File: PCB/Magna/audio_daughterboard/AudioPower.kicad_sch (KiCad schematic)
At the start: 24 parts, among them U901 TPS61040DBV, U902 AMS1117-5.0

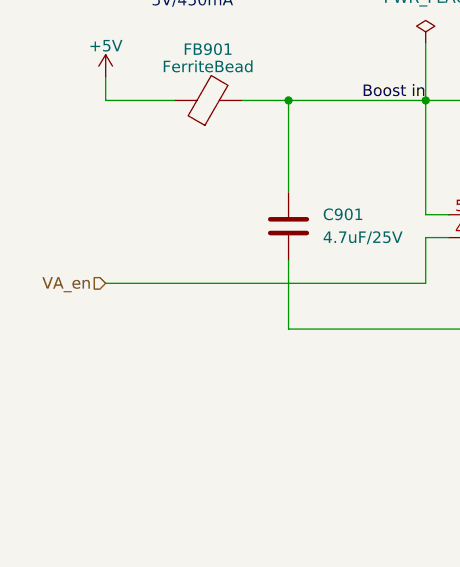
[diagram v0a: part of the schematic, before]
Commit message: Update connector on ADC board and clean up MCU sheet
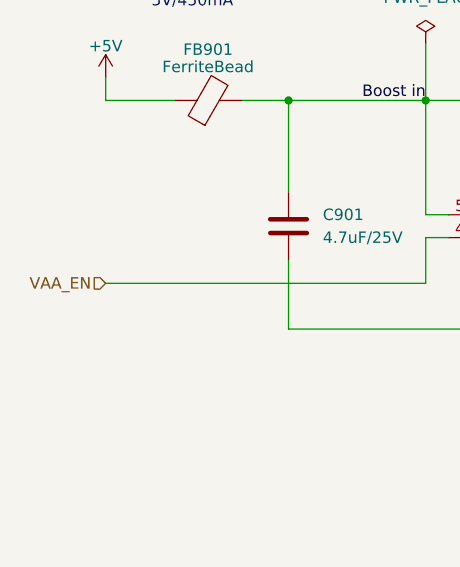
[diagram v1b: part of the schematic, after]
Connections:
- net VA_en renamed VAA_EN
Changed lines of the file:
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@@
     (effects (font (size 1.27 1.27)) (justify right bottom))
   )
-  (hierarchical_label "VA_en" (shape input) (at 26.67 129.54 180) (fields_autoplaced)
+  (hierarchical_label "VAA_EN" (shape input) (at 26.67 129.54 180) (fields_autoplaced)
     (effects (font (size 1.27 1.27)) (justify right))
   )

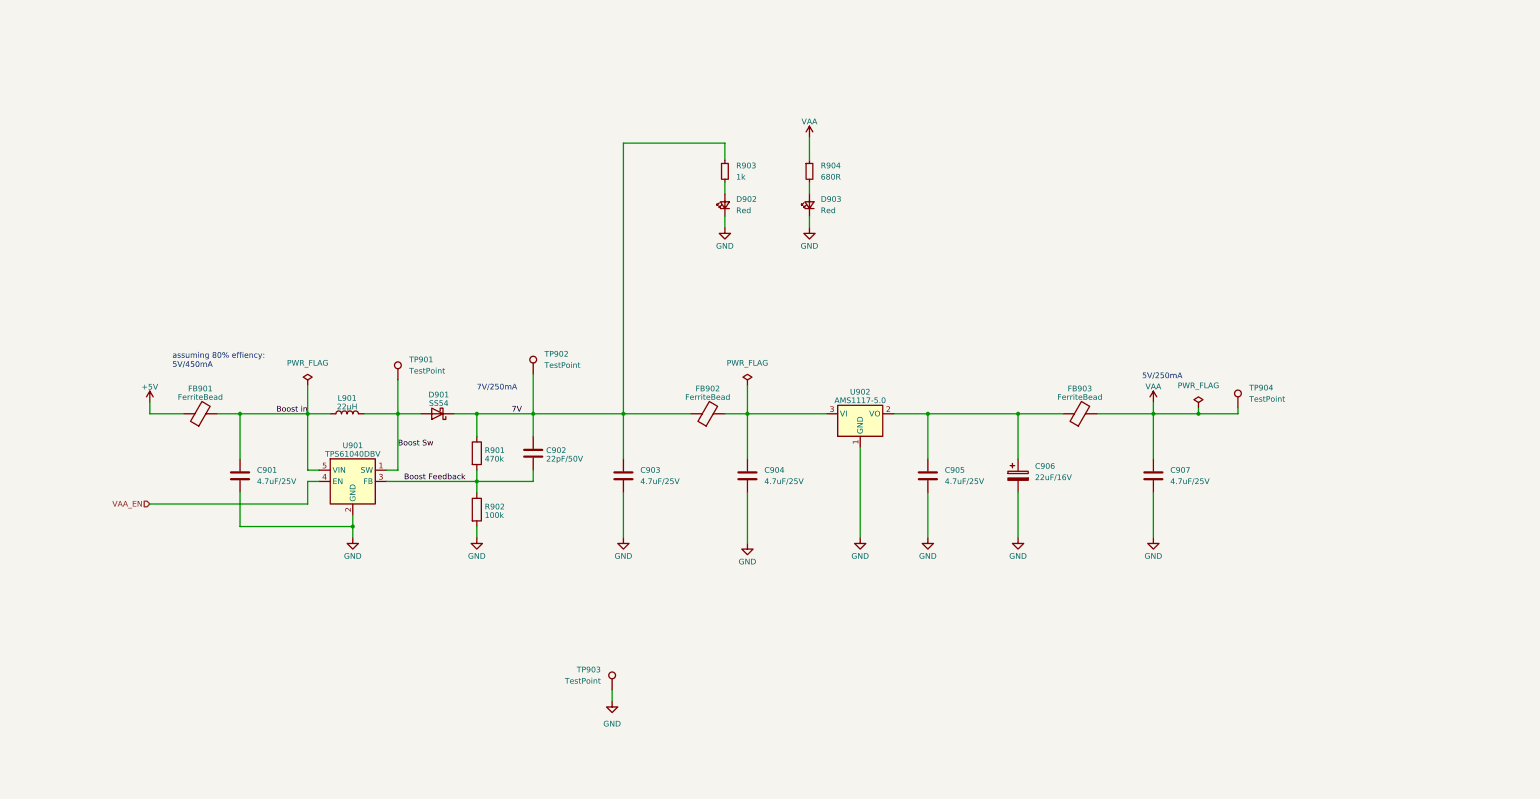
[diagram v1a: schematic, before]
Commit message: Start of redesign of Audio board
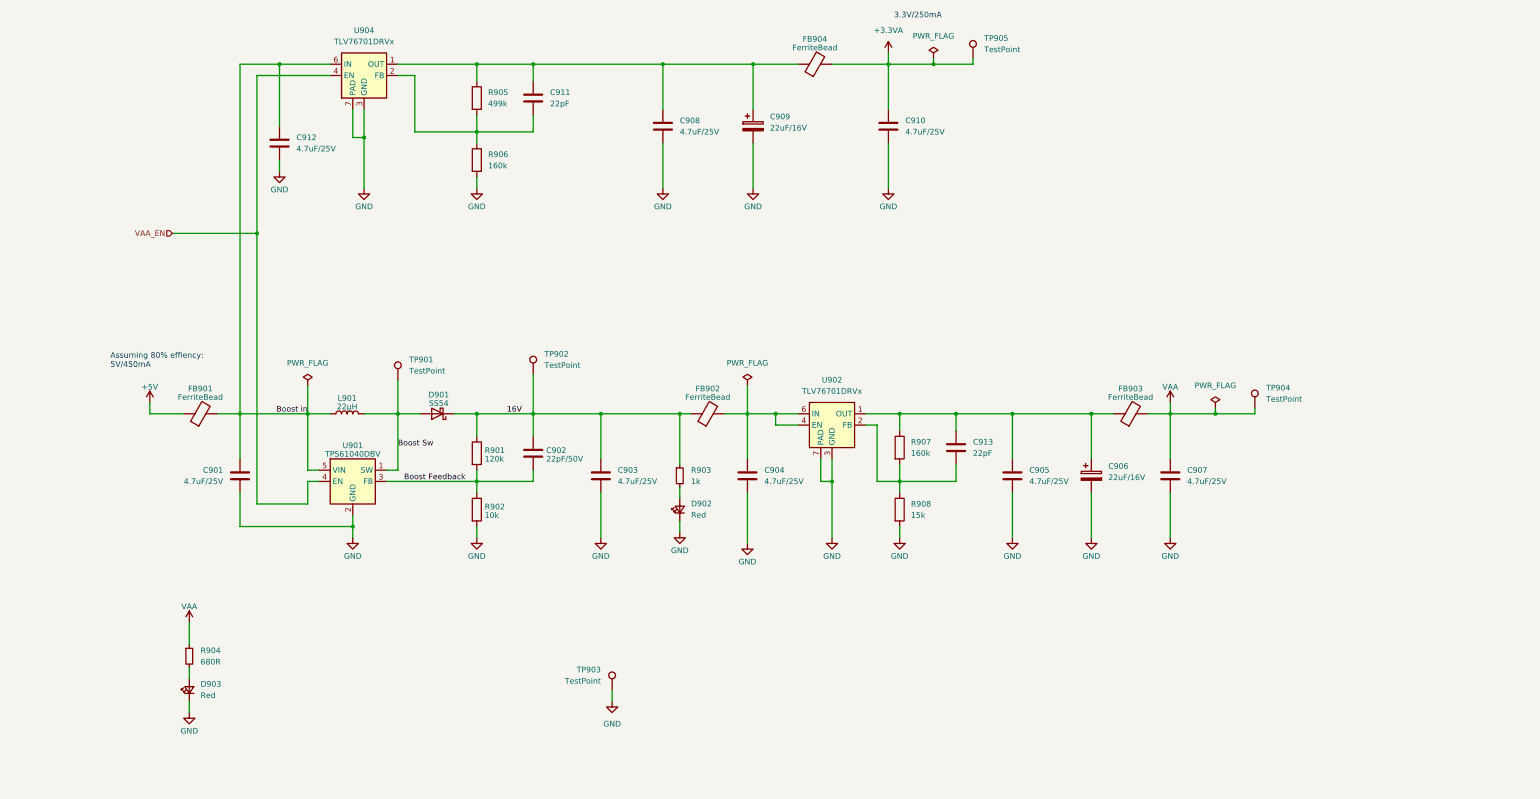
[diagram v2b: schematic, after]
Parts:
- removed U902: AMS1117-5.0, Package_TO_SOT_SMD:SOT-223-3_TabPin2, symbol Regulator_Linear:AMS1117-5.0
- added C908, C910, C912: 4.7uF/25V, Capacitor_SMD:C_0805_2012Metric_Pad1.18x1.45mm_HandSolder, symbol Device:C
- added C909: 22uF/16V, Capacitor_SMD:CP_Elec_5x5.8, symbol Device:C_Polarized
- added C911, C913: 22pF, symbol Device:C
- added FB904: FerriteBead, Inductor_SMD:L_0805_2012Metric, symbol Device:FerriteBead
- added R905: 499k, symbol Device:R
- added R906, R907: 160k, symbol Device:R
- added R908: 15k, symbol Device:R
- added TP905: TestPoint, TestPoint:TestPoint_Keystone_5005-5009_Compact, symbol Connector:TestPoint
- added U902, U904: TLV76701DRVx, Package_SON:WSON-6-1EP_2x2mm_P0.65mm_EP1x1.6mm_ThermalVias, symbol Regulator_Linear:TLV76701DRVx
- R901: value 470k -> 120k
- R902: value 100k -> 10k
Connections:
- net Boost in: now also C912.1, U904.6 (IN)
- net GND: now also C908.2, C909.2, C910.2, C912.2, R906.2, R908.2, U902.3 (GND), U902.5 (GND), U902.7 (PAD), U904.3 (GND), U904.5 (GND), U904.7 (PAD)
- net VAA_EN: now also U904.4 (EN)
- net at C905.1, C906.1, FB903.1: now also C913.1, R907.1, U902.1 (OUT)
- net at C904.1, FB902.2: now also U902.4 (EN), U902.6 (IN)
- net 7V renamed 16V
- new net: C908.1, C909.1, C911.1, FB904.1, R905.1, U904.1 (OUT)
- new net: C911.2, R905.2, R906.1, U904.2 (FB)
- new net: C913.2, R907.2, R908.1, U902.2 (FB)
- new net +3.3VA: C910.1, FB904.2, TP905.1
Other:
- note added: "3.3V/250mA"
- note added: "Assuming 80% effiency: 5V/450mA"
- note removed: "5V/250mA"
- note removed: "7V/250mA"
- note removed: "assuming 80% effiency: 5V/450mA"
- moved on the sheet: C903, C905, C906, C907, D902, D903, FB903, R903, R904, TP904

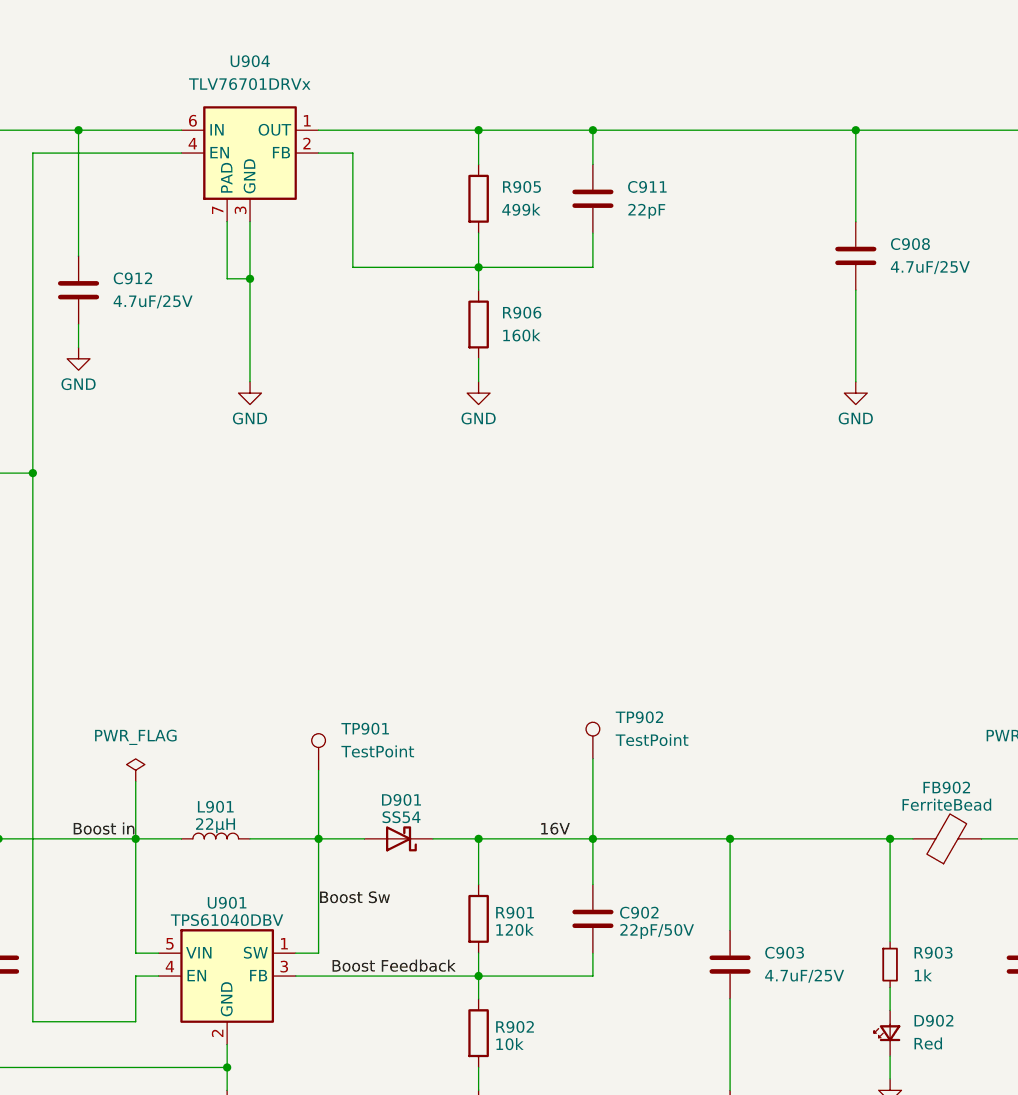
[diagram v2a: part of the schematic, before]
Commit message: Add simulation to all components
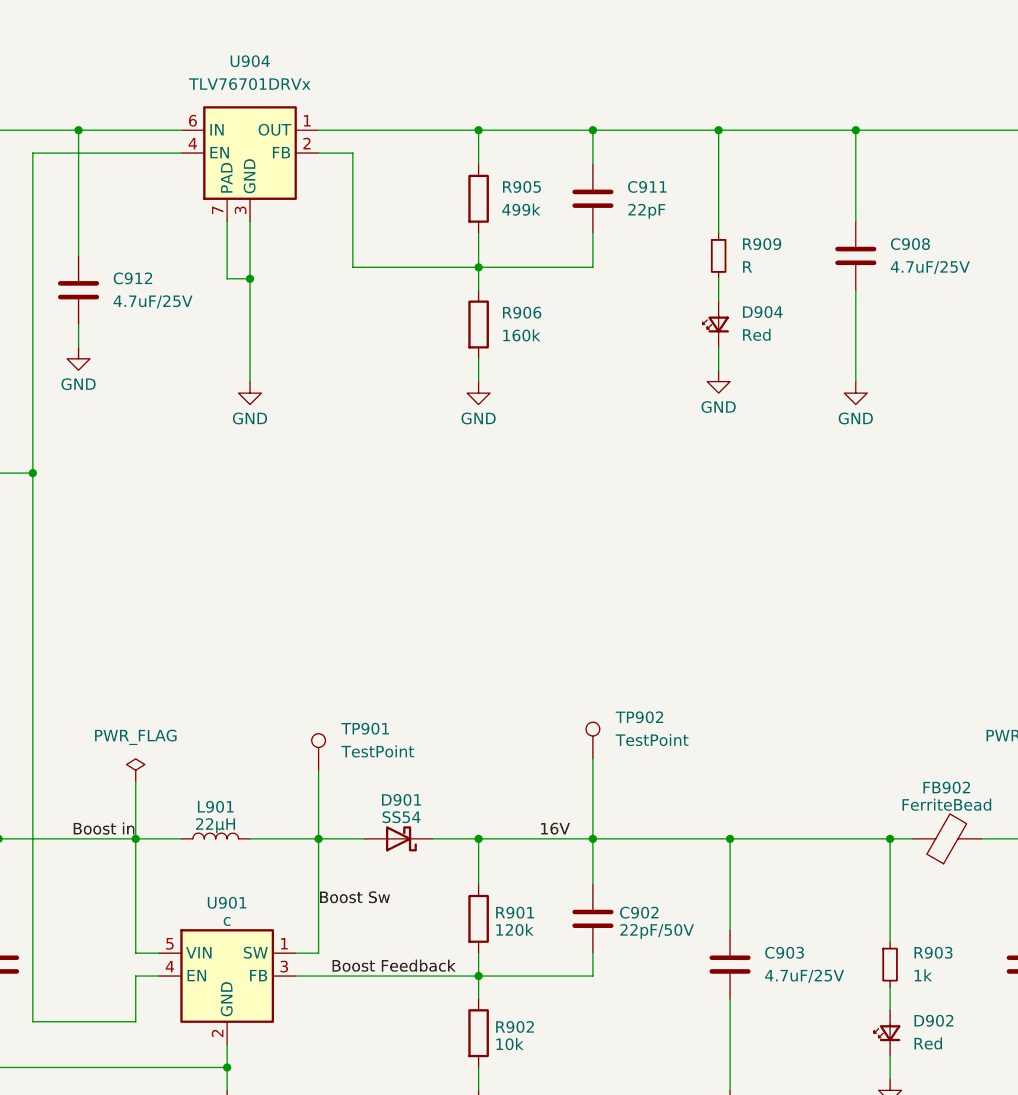
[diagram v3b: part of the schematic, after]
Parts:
- added D904: Red, Diode_SMD:D_0805_2012Metric_Pad1.15x1.40mm_HandSolder, symbol Device:LED_Small
- added R909: R, Resistor_SMD:R_0805_2012Metric_Pad1.20x1.40mm_HandSolder, symbol Device:R_Small
- U901: value TPS61040DBV -> c
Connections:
- net GND: now also D904.1 (K)
- net at C908.1, C909.1, C911.1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: now also R909.1
- new net: D904.2 (A), R909.2

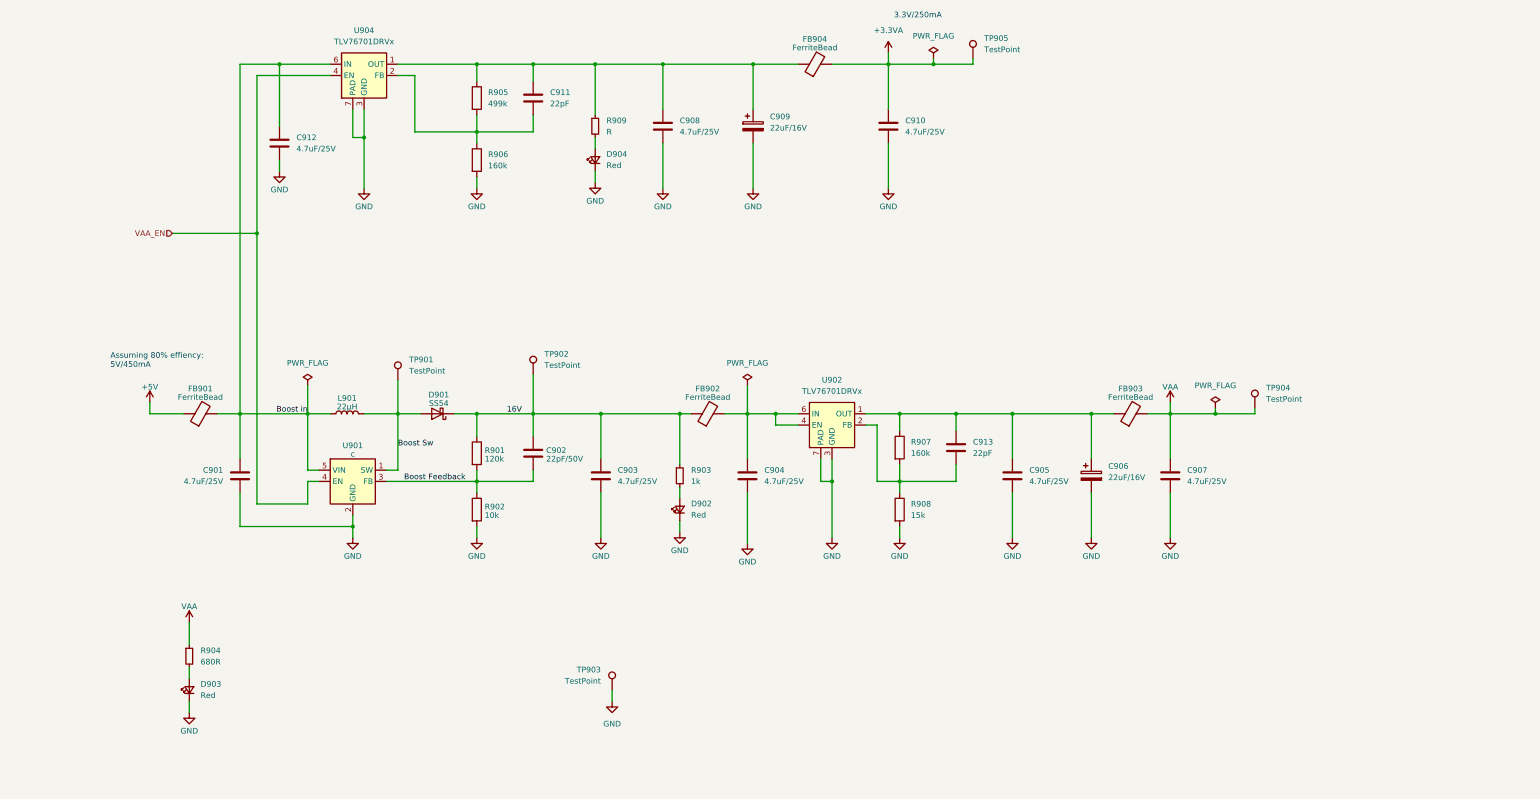
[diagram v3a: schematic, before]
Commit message: Finish simulations and design of input filtering
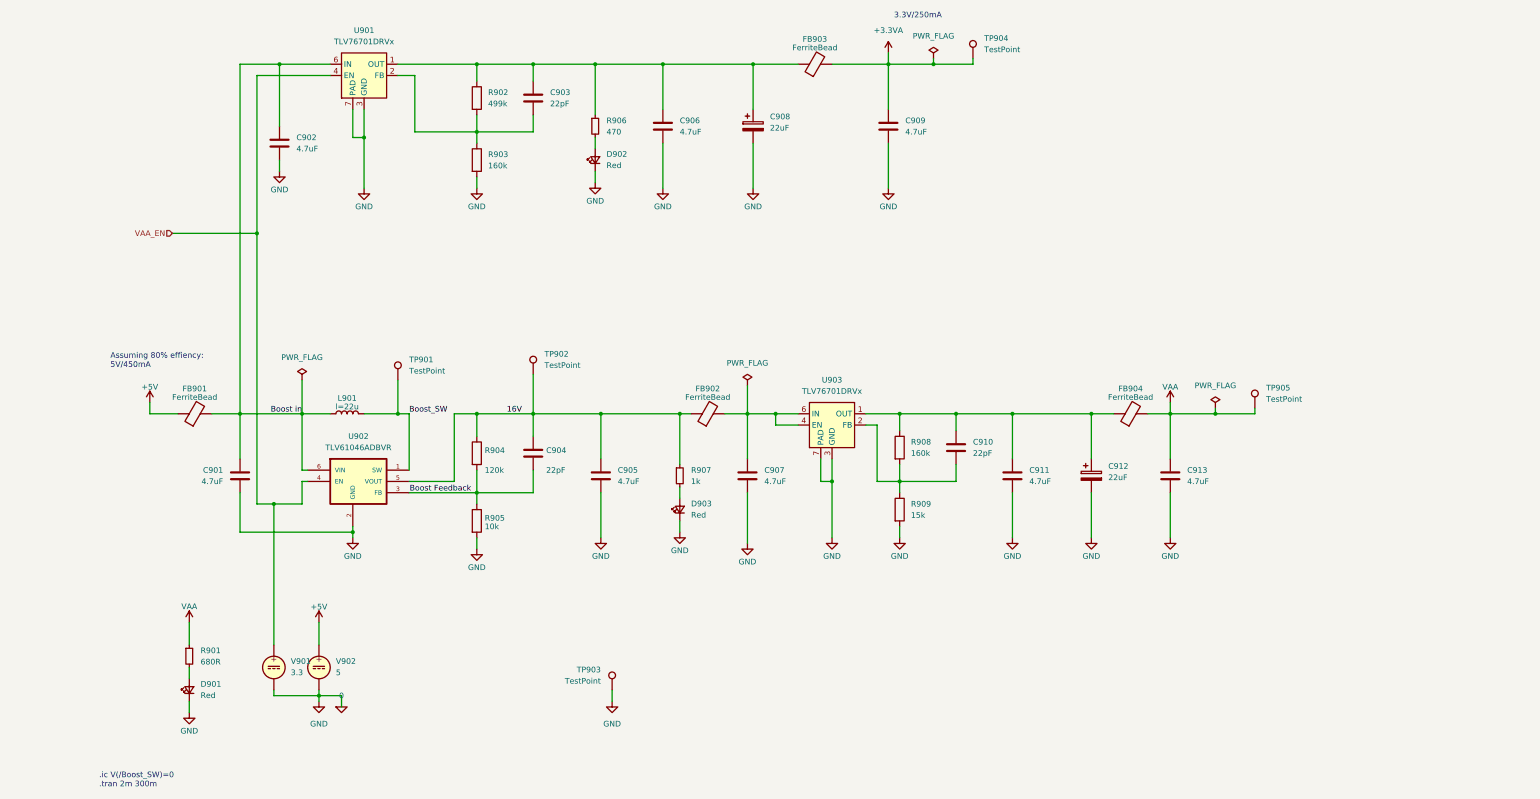
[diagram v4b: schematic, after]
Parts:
- removed D901: SS54, Diode_SMD:D_SMA_Handsoldering, symbol Device:D_Schottky
- removed U901: c, Package_TO_SOT_SMD:SOT-23-5, symbol Regulator_Switching:TPS61040DBV
- removed U902: TLV76701DRVx, Package_SON:WSON-6-1EP_2x2mm_P0.65mm_EP1x1.6mm_ThermalVias, symbol Regulator_Linear:TLV76701DRVx
- added U902: TLV61046ADBVR, TLV61046ADBVR:SOT95P280X145-6N, symbol Skrooter_symbols:TLV61046ADBVR
- added U903: TLV76701DRVx, Package_SON:WSON-6-1EP_2x2mm_P0.65mm_EP1x1.6mm_ThermalVias, symbol Regulator_Linear:TLV76701DRVx
- added V901: 3.3, symbol Simulation_SPICE:VDC
- added V902: 5, symbol Simulation_SPICE:VDC
- C901: value 4.7uF/25V -> 4.7uF; Votlage (none) -> 25V
- C902: renamed from C912; value 4.7uF/25V -> 4.7uF; Voltage (none) -> 25V
- C904: renamed from C902; value 22pF/50V -> 22pF; Voltage (none) -> 50V
- C905: renamed from C903; value 4.7uF/25V -> 4.7uF
- C906: renamed from C908; value 4.7uF/25V -> 4.7uF; Voltage (none) -> 25V
- C907: renamed from C904; value 4.7uF/25V -> 4.7uF
- C908: renamed from C909; value 22uF/16V -> 22uF; Voltage (none) -> 16V
- C909: renamed from C910; value 4.7uF/25V -> 4.7uF; Field5 (none) -> 25V
- C911: renamed from C905; value 4.7uF/25V -> 4.7uF
- C912: renamed from C906; value 22uF/16V -> 22uF
- C913: renamed from C907; value 4.7uF/25V -> 4.7uF
- L901: value 22µH -> ${SIM.PARAMS}
- R906: renamed from R909; value R -> 470
- renumbered C911 to C903, C913 to C910, D903 to D901, D904 to D902, D902 to D903, FB904 to FB903, FB903 to FB904, R904 to R901, R905 to R902, R906 to R903, R901 to R904, R902 to R905, R903 to R907, R907 to R908, R908 to R909, TP905 to TP904, TP904 to TP905, U904 to U901
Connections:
- net +5V: now also V902.1
- net 16V: now also U902.5 (VOUT)
- net Boost Feedback: now also U902.3 (FB)
- net Boost in: now also U902.6 (VIN)
- net VAA_EN: now also U902.4 (EN), V901.1
- net at C910.1, C911.1, C912.1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: now also U903.1 (OUT)
- net at C910.2, R908.2, R909.1: now also U903.2 (FB)
- net at C907.1, FB902.2: now also U903.4 (EN), U903.6 (IN)
- net Boost Sw renamed Boost_SW
- net Boost_SW: now also U902.1 (SW)
- net GND renamed 0
- net 0: now also U902.2 (GND), U903.3 (GND), U903.5 (GND), U903.7 (PAD), V901.2, V902.2
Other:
- note added: ".ic V(/Boost_SW)=0 .tran 2m 300m"
- moved on the sheet: R905
